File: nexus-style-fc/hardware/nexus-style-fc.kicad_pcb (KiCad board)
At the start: 6 copper layers, 22.4 x 33.1 mm, 88 parts, among them J1 Header child board, J2 DSM (UART1), J3 A-CRSF (UART4), J4 C (UART3), J5 B (UART6), J6 USB-C vertical, SW1 BOOT, U1 STM32F722RET6, U10 TPS70933DBVR, U11 SRV05-4, U12 SRV05-4, U13 SRV05-4, U14 TPS629210DRLR, U15 SRV05-4, U2 ICM-42688-P, U3 DPS368XTSA1, U4 W25N01GVZEIG, U5 TPS62130RGTR, U7 USBLC6-2SC6, U9 TPS2116DRLR, Y1 8MHz 20pF

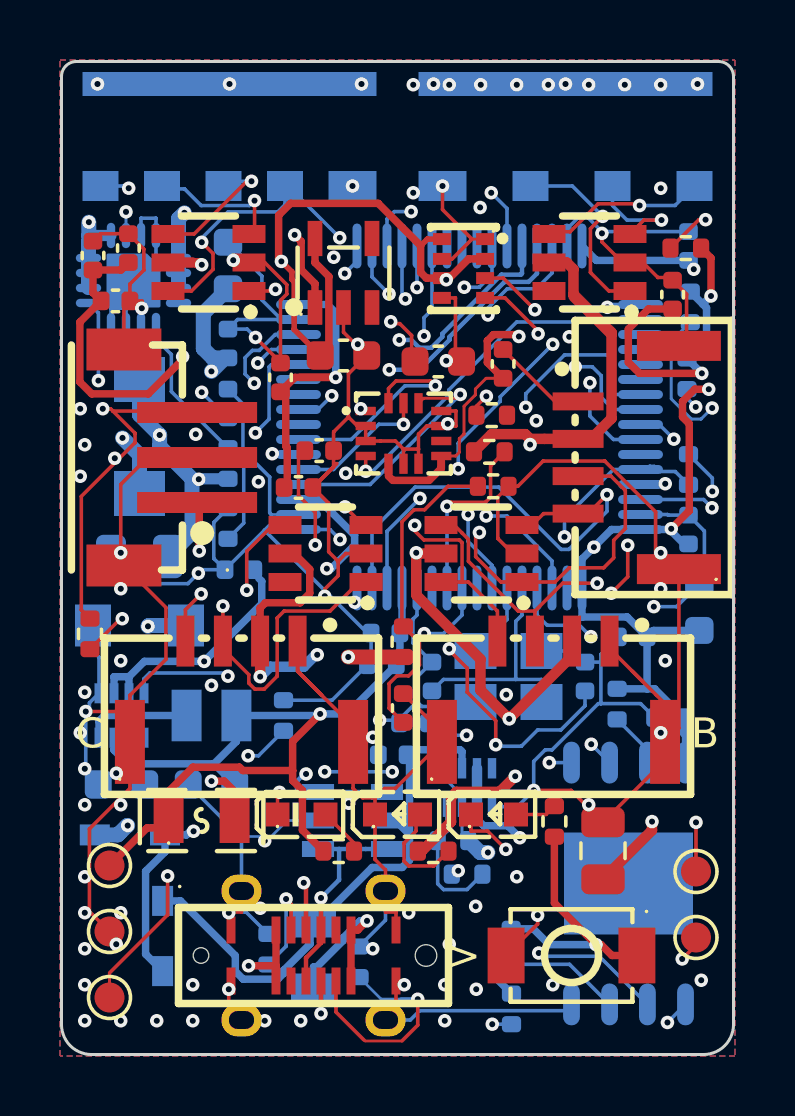
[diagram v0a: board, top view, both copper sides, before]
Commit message: Consolidate Nexus stage36 into canonical project paths
Preserve matched native sources and manufacturing bytes; use Git history for older project snapshots. Retain revision-bound validation evidence, document open release gates, and guard destructive regeneration.
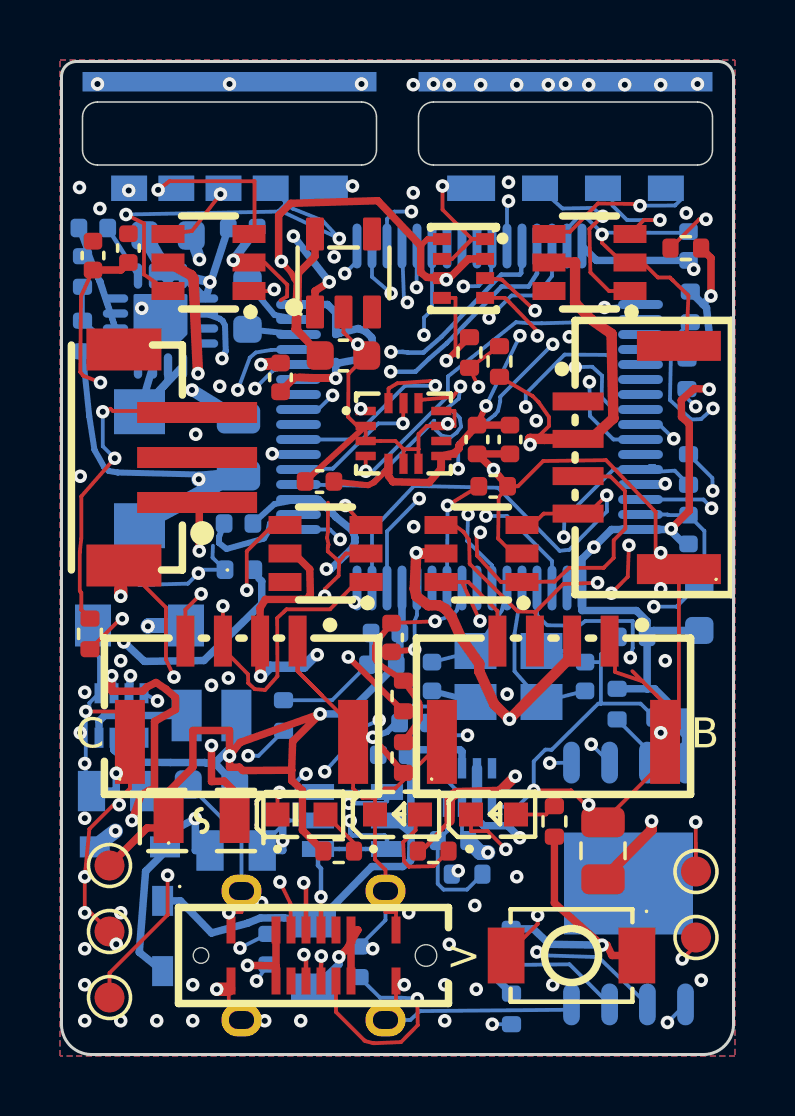
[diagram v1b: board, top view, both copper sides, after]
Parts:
- added C31: 22uF, NexusFC:C_0805_2012Metric_Samsung_CL21_MinLand, B.Cu at (105.8, 126.3)
- C1, C9: moved to B.Cu
- C27: value 4.7uF -> 22uF; footprint Capacitor_SMD:C_0603_1608Metric -> NexusFC:C_0805_2012Metric_Samsung_CL21_MinLand
- D1: footprint NexusFC:LED0603-RD_GREEN -> NexusFC:LED0603-RD_GREEN__NexusMain_D1
- D2: footprint NexusFC:LED0603-RD_RED -> NexusFC:LED0603-RD_RED__NexusMain_D2
- D3: footprint NexusFC:LED0603-RD_BLUE -> NexusFC:LED0603-RD_BLUE__NexusMain_D3
- J4: footprint NexusFC:CONN-SMD_4P-P1.25_BM04B-GHS-TBT-LF-SN -> NexusFC:CONN-SMD_4P-P1.25_BM04B-GHS-TBT-LF-SN__NexusMain_J4
- J6: footprint NexusFC:USB-C-SMD_TYPE-C-31-D-06 -> NexusFC:USB-C-SMD_TYPE-C-31-D-06__NexusMain_J6
- U10: footprint NexusFC:SOT-23-5_L3.0-W1.7-P0.95-LS2.8-BL -> NexusFC:TPS70933DBVR_TI_DBV0005A
- moved R12 9.70 mm to (100.7, 107.0)
- moved R17 9.52 mm to (111.4, 123.2), turned to -90 degrees
- moved C15 9.08 mm to (108.6, 114.0), turned to 180 degrees
- moved C23 7.37 mm to (101.1, 105.5), turned to 180 degrees
- moved C14 7.26 mm to (115.0, 112.6), turned to -90 degrees
- moved C9 6.62 mm to (106.2, 108.2), turned to 90 degrees
- moved R11 6.45 mm to (100.7, 109.2)
- moved C30 5.92 mm to (114.4, 114.2)
- moved C11 5.10 mm to (117.5, 120.5)
- moved C12 5.10 mm to (112.3, 120.5), turned to -90 degrees
- moved C24 4.92 mm to (105.9, 112.8), turned to 90 degrees
- moved C22 3.88 mm to (106.0, 105.5), turned to 0 degrees
- moved R18 3.03 mm to (114.6, 110.0), turned to 90 degrees
- moved C13 2.67 mm to (113.8, 112.6), turned to -90 degrees
- moved C29 2.38 mm to (111.0, 119.2), turned to -90 degrees
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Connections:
- net USB_DM renamed USB_DN
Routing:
- net VSYS: track 43.8 -> 64.5 mm, vias 3 -> 7
- net VCAP: track 15.1 -> 1.71 mm, vias 3 -> 0
- net GND: track 225.1 -> 212.4 mm, vias 75 -> 78
- net 5V_SENSE: track 20.1 -> 10.2 mm, vias 3 -> 2
- net OSC_OUT: track 11.6 -> 3.88 mm, vias 2 -> 0
- net SW_5V: track 13.0 -> 5.59 mm, vias 2 -> 0
- net SBUS: track 20.7 -> 27.2 mm
- net 3V3: track 126.0 -> 132.4 mm, vias 8 -> 9
- net FB_5V: track 8.54 -> 2.48 mm
- net TAIL: track 23.8 -> 29.6 mm
- net SS_5V: track 7.56 -> 1.89 mm, vias 2 -> 0
- net VX_SENSE: track 13.5 -> 8.03 mm
- net 5V: track 84.0 -> 88.6 mm
- net RPM: track 20.1 -> 24.4 mm
- net DSM_TX: track 37.4 -> 41.5 mm
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
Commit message: fix(nexus): clean up native fabrication warnings and bind verified exports
Center existing via connections, fix mixed USB connector classification,
move conflicting outline artwork to Fab layers, and synchronize reviewed
symbol/footprint identities. Preserve accepted pads, pinouts and parts.

Regenerate main CAM and record full KiCad 10 ERC/DRC/parity and source/CAM
consistency evidence. Keep remaining factory and bench qualification gates
explicit; this checkpoint is not a fabrication or flight release.
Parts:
- F1: footprint NexusFC:F0805 -> NexusFC:F0805__NexusMain_F1
- F2: footprint NexusFC:F0805 -> NexusFC:F0805__NexusMain_F2
- J2: footprint NexusFC:CONN-SMD_B3B-ZR-SM4-TF -> NexusFC:CONN-SMD_B3B-ZR-SM4-TF__NexusMain_J2
- J3: footprint NexusFC:CONN-SMD_4P-P1.25_BM04B-GHS-TBT-LF-SN -> NexusFC:CONN-SMD_4P-P1.25_BM04B-GHS-TBT-LF-SN__NexusMain_J3
- J5: footprint NexusFC:CONN-SMD_4P-P1.25_BM04B-GHS-TBT-LF-SN -> NexusFC:CONN-SMD_4P-P1.25_BM04B-GHS-TBT-LF-SN__NexusMain_J5
- L2: footprint NexusFC:IND-SMD_L2.0-W1.6 -> NexusFC:IND-SMD_L2.0-W1.6__NexusMain_L2
- R2: footprint Resistor_SMD:R_0402_1005Metric -> NexusFC:R_0402_1005Metric__NexusMain_R2
- R4: footprint Resistor_SMD:R_0402_1005Metric -> NexusFC:R_0402_1005Metric__NexusMain_R4
- Y1: footprint NexusFC:CRYSTAL-SMD_4P-L3.2-W2.5-BL -> NexusFC:CRYSTAL-SMD_4P-L3.2-W2.5-BL__NexusMain_Y1

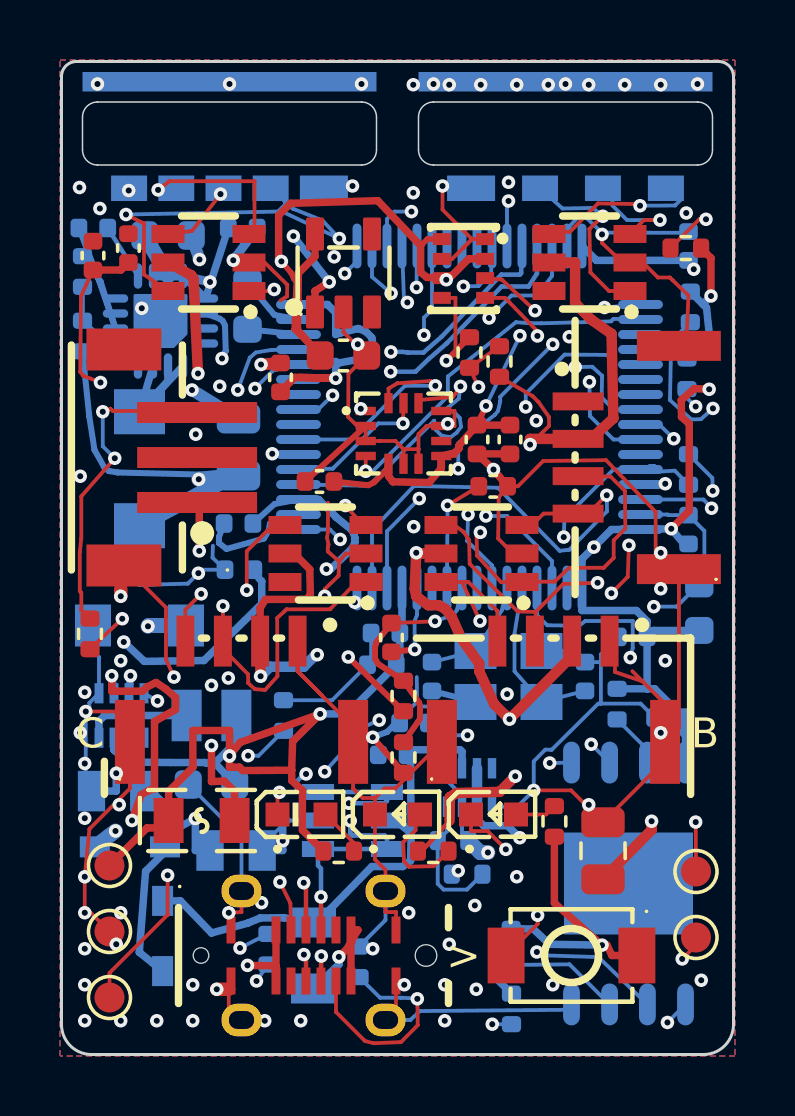
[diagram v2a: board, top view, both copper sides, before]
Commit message: tidy up traces
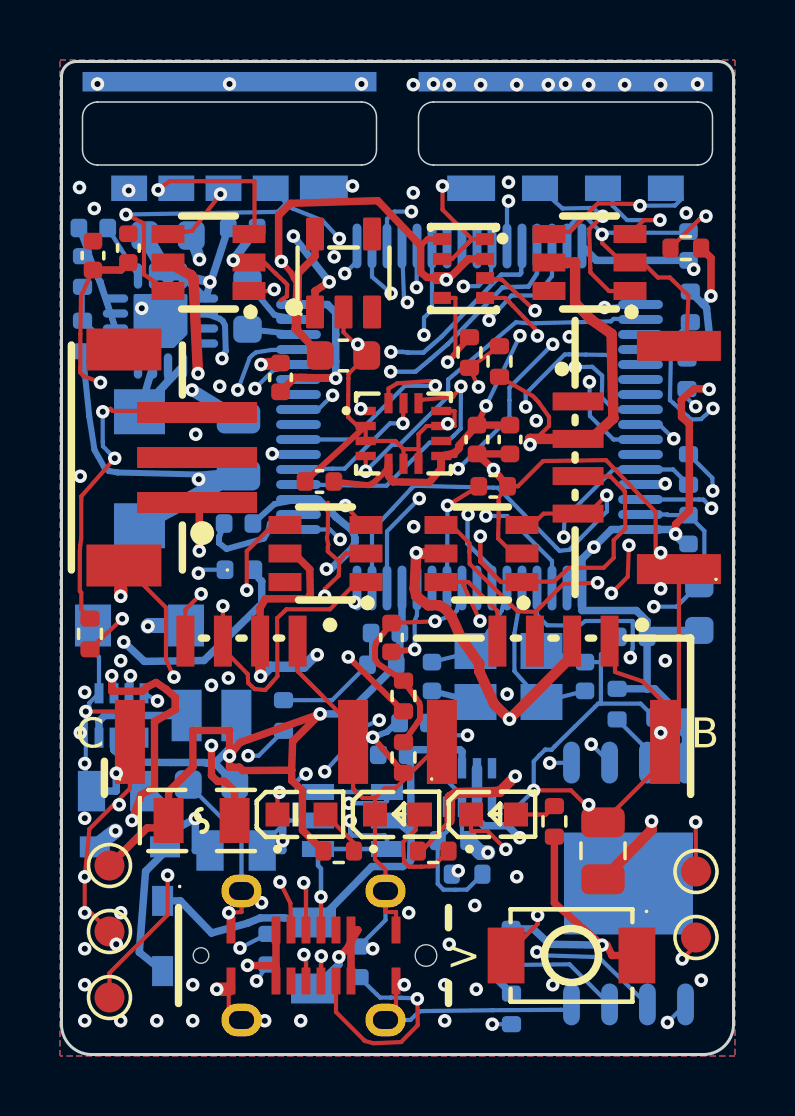
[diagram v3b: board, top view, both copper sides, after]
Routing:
- net GND: track 212.5 -> 202.3 mm
- net SBUS: track 27.2 -> 21.5 mm
- net 5V: track 88.6 -> 83.5 mm
- net DSM_DATA: track 63.8 -> 60.3 mm
- net TAIL: track 29.6 -> 27.4 mm
- net 3V3: track 132.5 -> 130.9 mm
- net VSYS: track 64.5 -> 63.0 mm
- net IMU_CS: track 29.4 -> 28.5 mm
